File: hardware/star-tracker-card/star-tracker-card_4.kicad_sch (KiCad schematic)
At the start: 37 parts, among them U1 RCLAMP0504FB, U7 OSD3358-512M-BSM, Y1 24MHz, Y2 ABS07-32.768KHZ-T

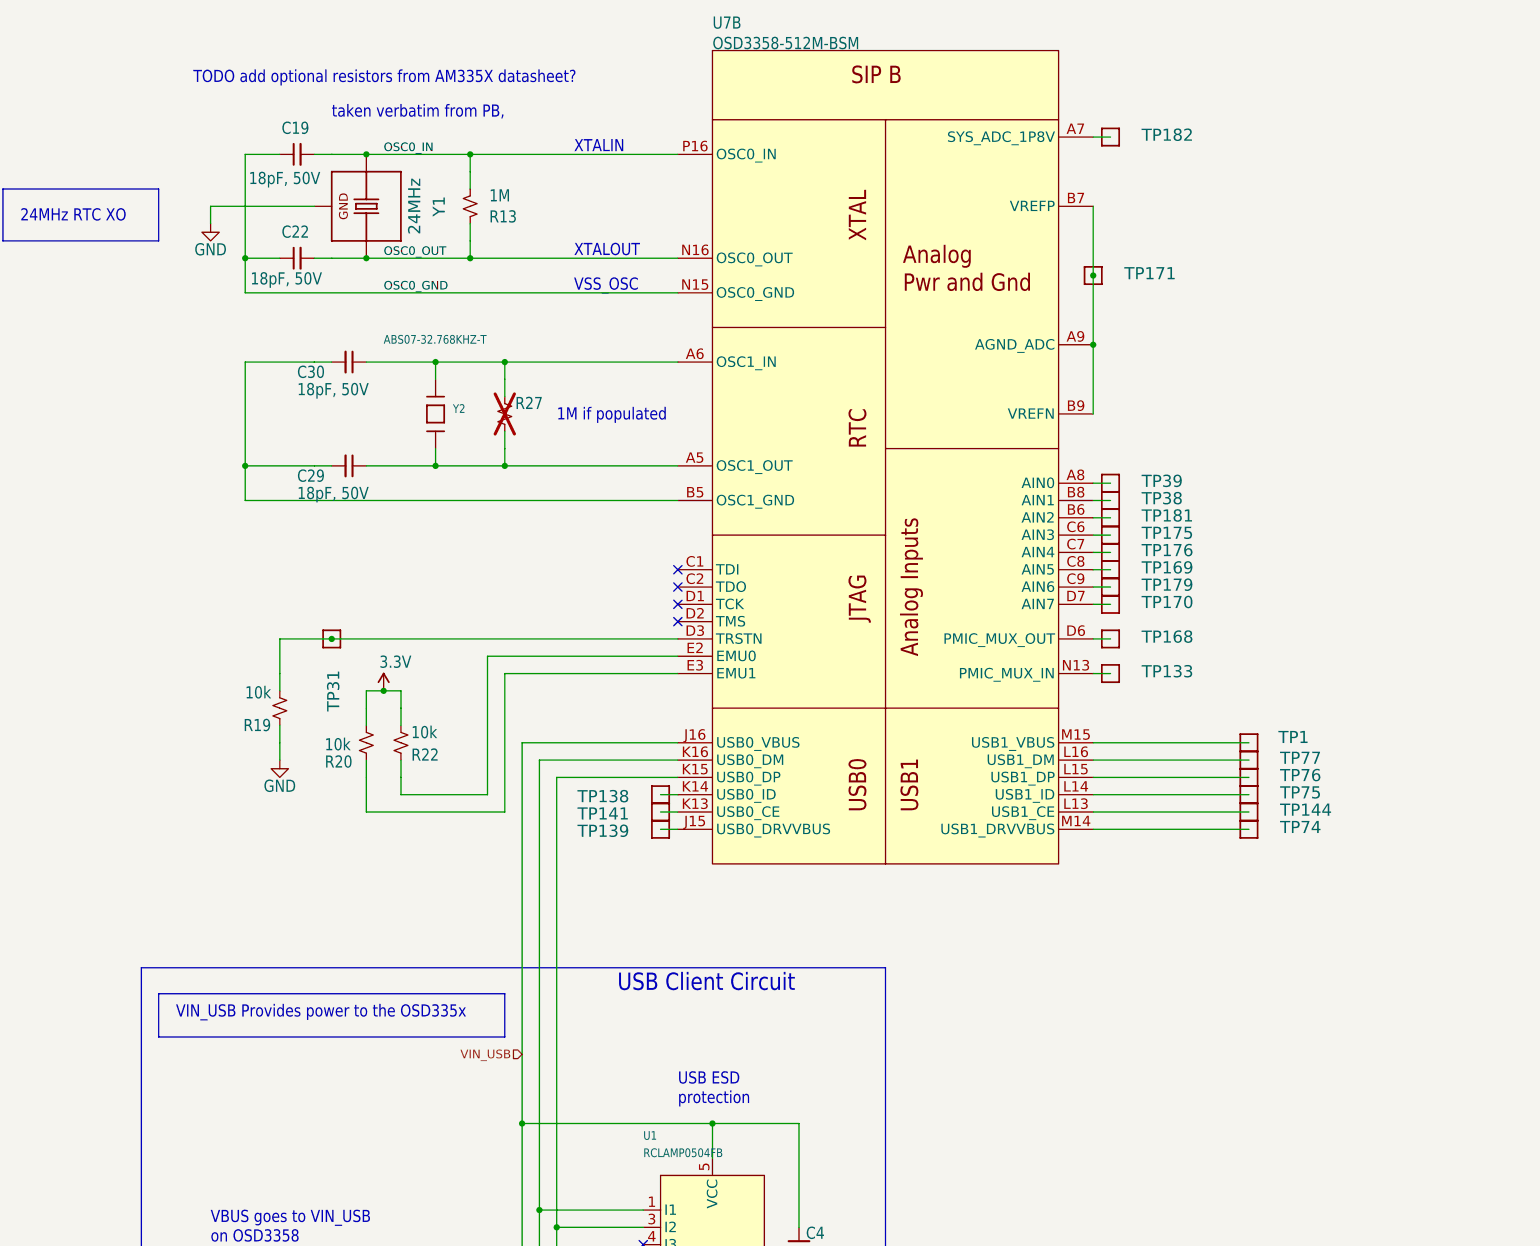
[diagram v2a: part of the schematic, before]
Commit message: Updated Octavo schematic
Removed many testpoints, added filter to 1.8v reference, tied some signals to ground with pull down resistor, added NCs to multiple pins.
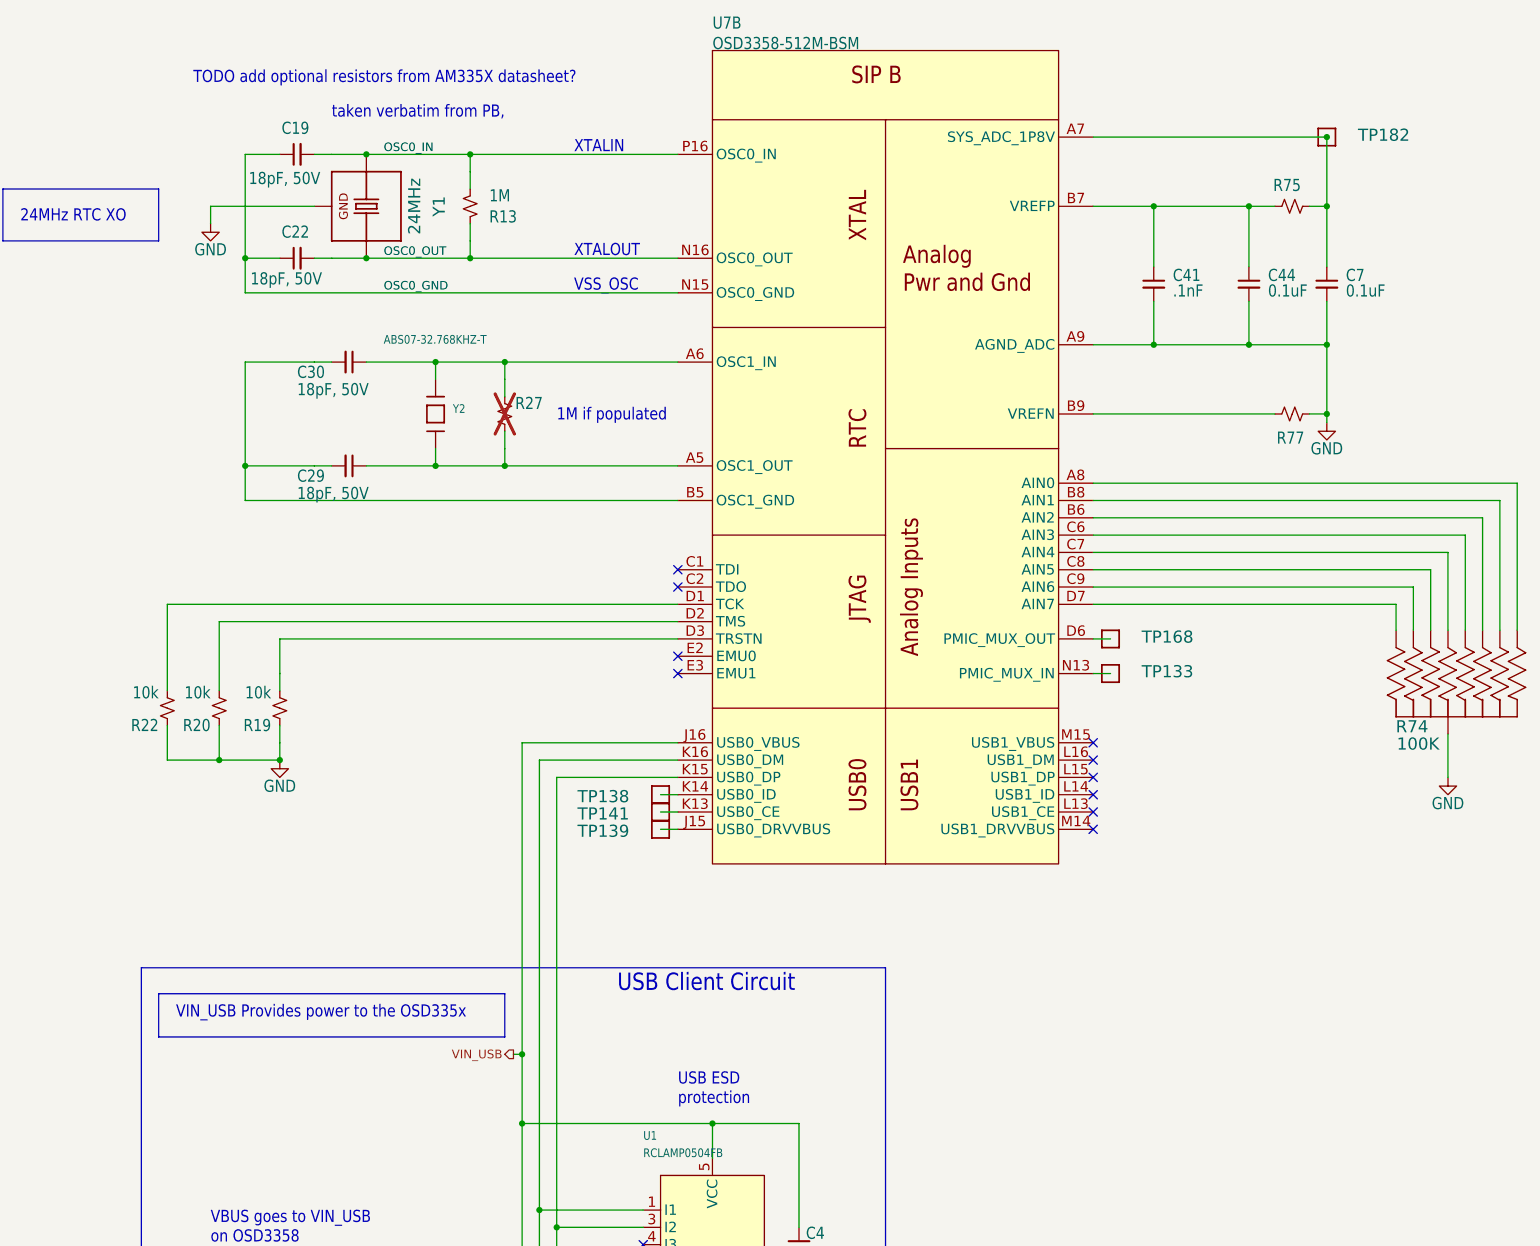
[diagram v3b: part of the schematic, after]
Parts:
- removed TP1, TP144, TP169, TP170, TP171, TP175, TP176, TP179, TP181, TP31, TP38, TP39, TP74, TP75, TP76, TP77: TEST-POINT3X4, oresat-misc:TestPoint_Pad_D1.0mm, symbol oresat-misc:Test-Point-1mm-round
- added C41: .1nF, oresat-passives:c_0603-SMALL, symbol Device:C_Small
- added C44, C7: 0.1uF, oresat-passives:c_0603-SMALL, symbol Device:C_Small
- added R74: 100K, star-tracker-card:ARRAY_EXBA-M, symbol star-tracker-card-eagle-import:EXB-A10P391JC_ARRAY_EXBA-M
- added R75, R77: 0, Resistor_SMD:R_0603_1608Metric, symbol Device:R_Small_US
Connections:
- net GND: now also R20.1, R22.1, U7.A9 (AGND_ADC), C41.2, C44.2, C7.2, R74.10 (55), R74.5 (55), R77.2
- net at U7.B8 (AIN1): now also R74.9 (99)
- net at U7.E2 (EMU0): no longer R22.1
- net at TP182.1, U7.A7 (SYS_ADC_1P8V): now also C7.1, R75.2
- net at U7.C6 (AIN3): now also R74.8 (88)
- net at U7.D7 (AIN7): now also R74.6 (66)
- net at U7.C7 (AIN4): now also R74.3 (33)
- net at U7.A8 (AIN0): now also R74.1 (11)
- net at U7.C9 (AIN6): now also R74.4 (44)
- net at U7.B6 (AIN2): now also R74.2 (22)
- net at U7.C8 (AIN5): now also R74.7 (77)
- net at U7.D1 (TCK): now also R22.2
- net at U7.D2 (TMS): now also R20.2
- net at U7.E3 (EMU1): no longer R20.1
- removed net 3.3V: R20.2, R22.2
- new net: C41.1, C44.1, R75.1, U7.B7 (VREFP)
- new net: R77.1, U7.B9 (VREFN)
- no-connect marks 6 -> 12
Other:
- moved on the sheet: TP182

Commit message: Update
Update to the octavo schematic
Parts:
- removed Y1: 24MHz, star-tracker-card:5X3.2-4SMD, symbol star-tracker-card-eagle-import:ECS-240-12-30BQ-AEN-TR
- removed Y2: ABS07-32.768KHZ-T, star-tracker-card:CRYSTAL_3.2X1.5, symbol star-tracker-card-eagle-import:ABS07-32.768KHZ-T
- added Y1: ECS-240-12-30BQ-AEN-TR, oresat-passives:CRYSTAL-5X3.2-4SMD, symbol Device:Crystal_GND24
- added Y2: ABS07-32.768KHZ-T, oresat-passives:CRYSTAL_3.2X1.5, symbol Device:Crystal
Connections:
- net OSC0_GND: now also Y1.2 (G), Y1.4 (G)
- net OSC0_IN: now also Y1.1
- net OSC0_OUT: now also Y1.3
- net at C29.1, R27.1, U7.A5 (OSC1_OUT): now also Y2.1
- net at C30.1, R27.2, U7.A6 (OSC1_IN): now also Y2.2
- net nRESET: now reaches U1.4 (I3)
- net VIN_USB: no longer names the net of C4.1, FB2.2, U1.5 (VCC), U7.J16 (USB0_VBUS)
- no-connect marks 12 -> 11
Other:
- note removed: "See Connectors Sheet"
- note removed: "VIN_USB Provides power to the OSD335x"
- moved on the sheet: FB2, R19, R20, R22

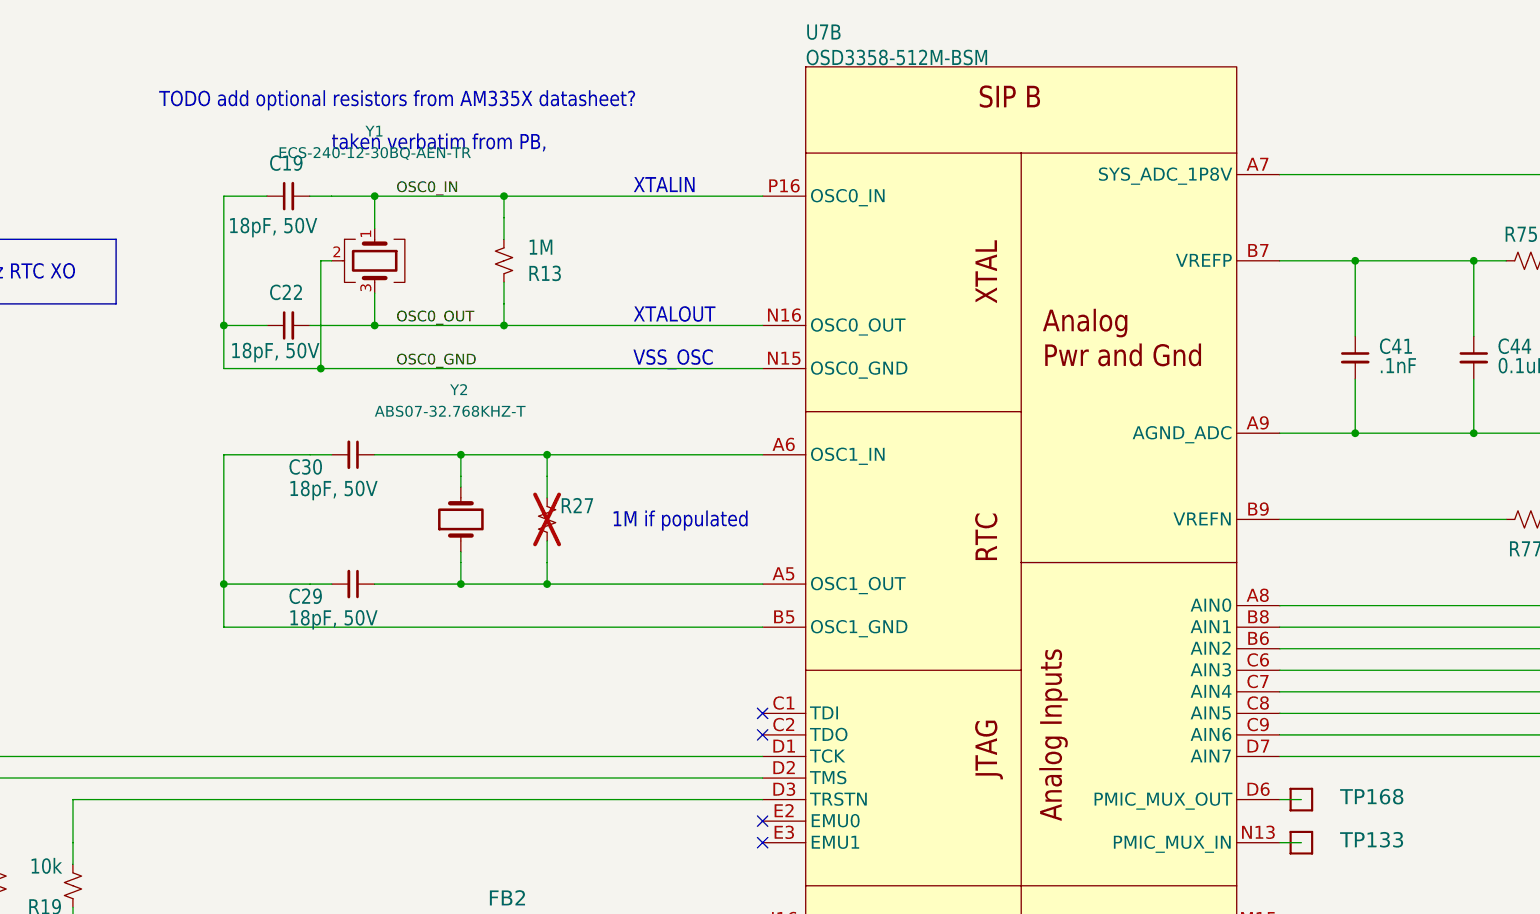
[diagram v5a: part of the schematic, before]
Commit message: Small Update
Removed couple more test points added 2 100nF caps and added text to out put possible pins connected to pull down resistors.
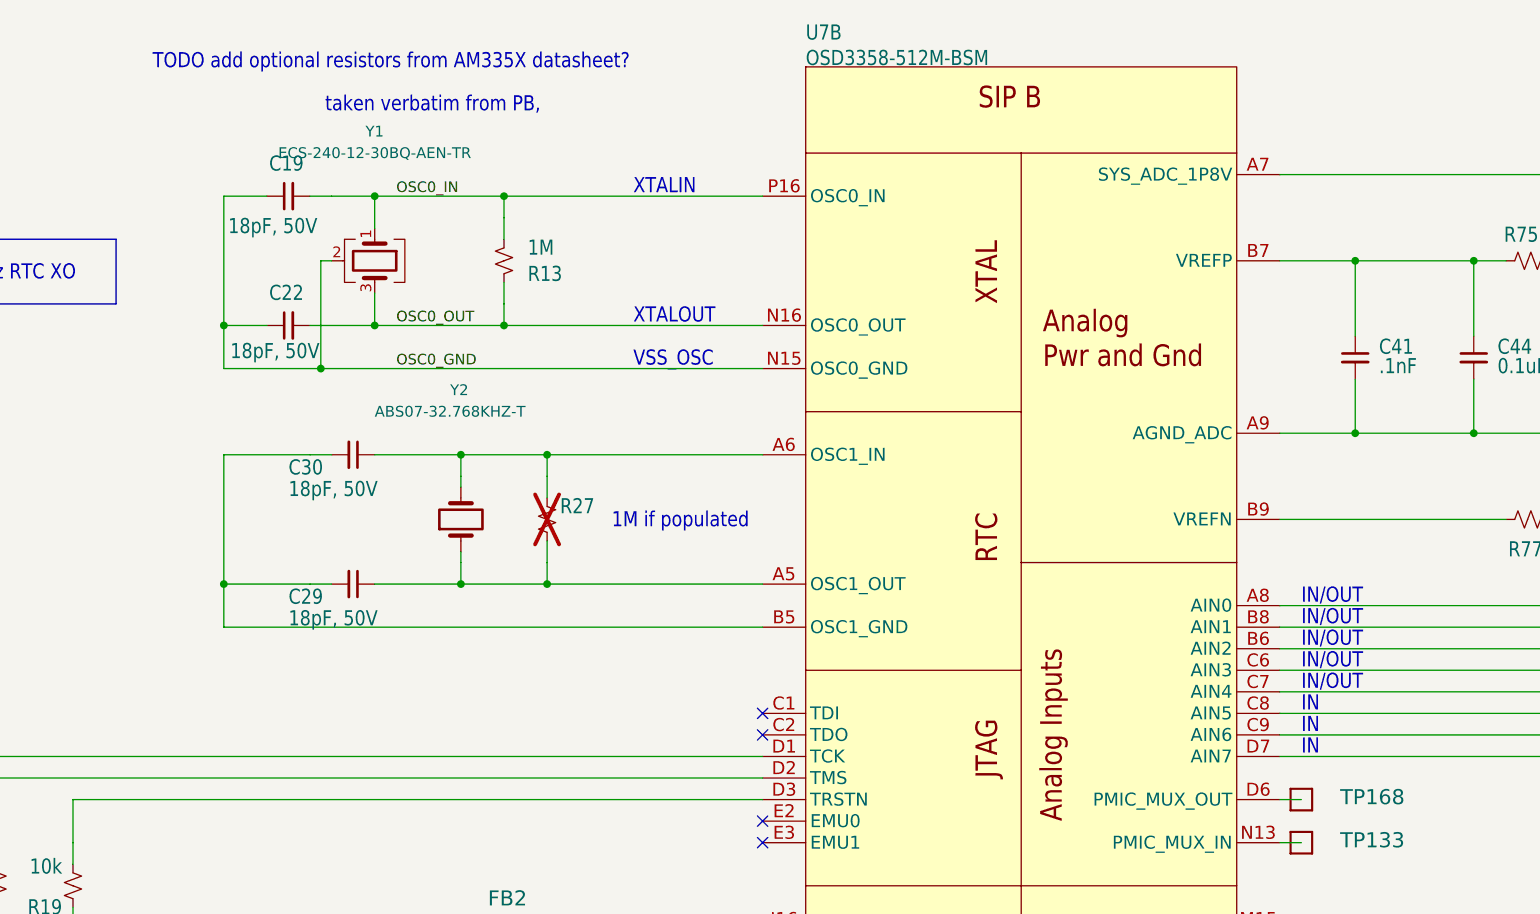
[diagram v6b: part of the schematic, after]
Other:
- note added: "IN"
- note added: "IN/OUT"
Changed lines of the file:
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@@
 		(company "Portland State Aerospace Society")
+	)
+	(text "IN/OUT"
+		(exclude_from_sim no)
+		(at 251.46 101.6 0)
+		(effects
+			(font
+				(size 1.778 1.5113)
+			)
+			(justify left bottom)
+		)
+	)
+	(text "IN"
+		(exclude_from_sim no)
+		(at 251.46 116.84 0)
+		(effects
+			(font
+				(size 1.778 1.5113)
+			)
+			(justify left bottom)
+		)
 	)
 	(text "USB ESD\nprotection"
 		(exclude_from_sim no)
 		(at 187.96 193.04 0)
+		(effects
+			(font
+				(size 1.778 1.5113)
+			)
+			(justify left bottom)
+		)
+	)
+	(text "IN"
+		(exclude_from_sim no)
+		(at 251.46 119.38 0)
+		(effects
+			(font
+				(size 1.778 1.5113)
+			)
+			(justify left bottom)
+		)
+	)
+	(text "IN/OUT"
+		(exclude_from_sim no)
+		(at 251.46 104.14 0)
 		(effects
 			(font
@@
 	(text "TODO add optional resistors from AM335X datasheet?"
 		(exclude_from_sim no)
-		(at 116.84 43.18 0)
+		(at 116.078 38.608 0)
 		(effects
 			(font
@@
 		)
 	)
+	(text "IN/OUT"
+		(exclude_from_sim no)
+		(at 251.46 106.68 0)
+		(effects
+			(font
+				(size 1.778 1.5113)
+			)
+			(justify left bottom)
+		)
+	)
 	(text "taken verbatim from PB,"
 		(exclude_from_sim no)
-		(at 137.16 48.26 0)
+		(at 136.398 43.688 0)
 		(effects
 			(font
@@
 		(effects
 			(font
+				(size 1.778 1.5113)
+			)
+			(justify left bottom)
+		)
+	)
+	(text "IN/OUT"
+		(exclude_from_sim no)
+		(at 251.46 111.76 0)
+		(effects
+			(font
+				(size 1.778 1.5113)
+			)
+			(justify left bottom)
+		)
+	)
+	(text "IN/OUT"
+		(exclude_from_sim no)
+		(at 251.46 109.22 0)
+		(effects
+			(font
+				(size 1.778 1.5113)
+			)
+			(justify left bottom)
+		)
+	)
+	(text "IN"
+		(exclude_from_sim no)
+		(at 251.46 114.3 0)
+		(effects
+			(font
